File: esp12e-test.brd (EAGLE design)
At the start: 22.5 x 30.5 mm, 12 parts, among them IC1 ESP-12E/F, U8 NCP1117LPST50T3G

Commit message: Add button and STEMMA connectors to esp12e-test board
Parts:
- added JP1, JP2: (no value), microbuilder:1X04_1.0MM
- added U$1: AMAZON_BUTTON, 00jim:AMAZON_BUTTON
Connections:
- net GND: now also JP1.1, JP2.1, U$1.2, U$1.3
- net IO00: now also U$1.1, U$1.4
- net SCL: now also JP1.4, JP2.4
- net SDA: now also JP1.3, JP2.3
- net VCC: now also JP1.2, JP2.2
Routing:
- net IO00: track 29.0 -> 62.0 mm, vias 2 -> 1
- net VCC: track 54.7 -> 84.9 mm, vias 1 -> 4
- net GND: track 32.2 -> 58.0 mm, vias 2 -> 6
- net SCL: track 19.4 -> 39.5 mm, vias 0 -> 2
- net SDA: track 19.2 -> 33.0 mm, vias 0 -> 1
- net EN: track 26.6 -> 34.4 mm
- net RXI: track 26.0 -> 33.7 mm, vias 1 -> 0
- net TXO: track 28.3 -> 21.3 mm
- net IO15: track 23.4 -> 24.9 mm
- net RST: track 26.9 -> 26.2 mm
- net RAW: track 20.8 -> 20.2 mm, vias 1 -> 2
- net IO02: track 14.0 -> 14.2 mm, vias 2 -> 0
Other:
- board size 22.5 x 30.5 mm -> 27.6 x 30.5 mm

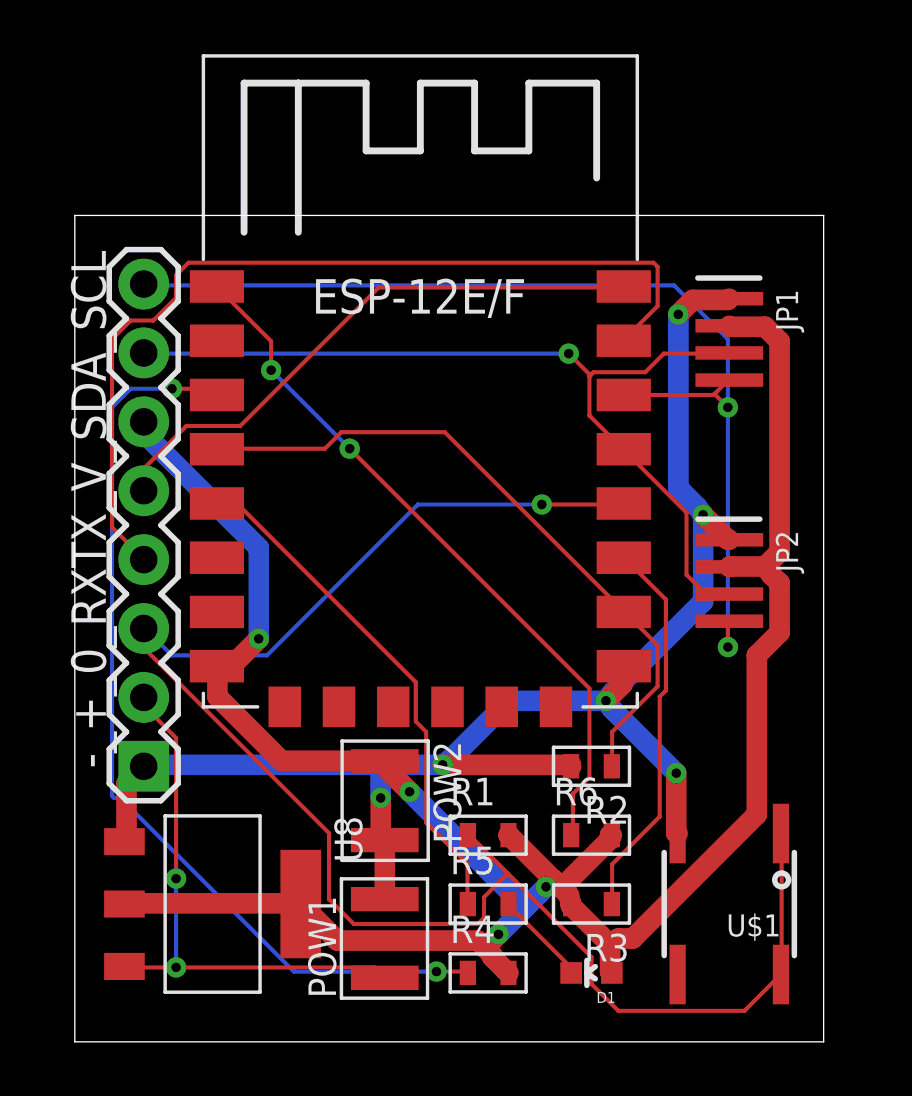
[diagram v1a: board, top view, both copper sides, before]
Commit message: Fix IO16 bug, change to better stemma-st connector
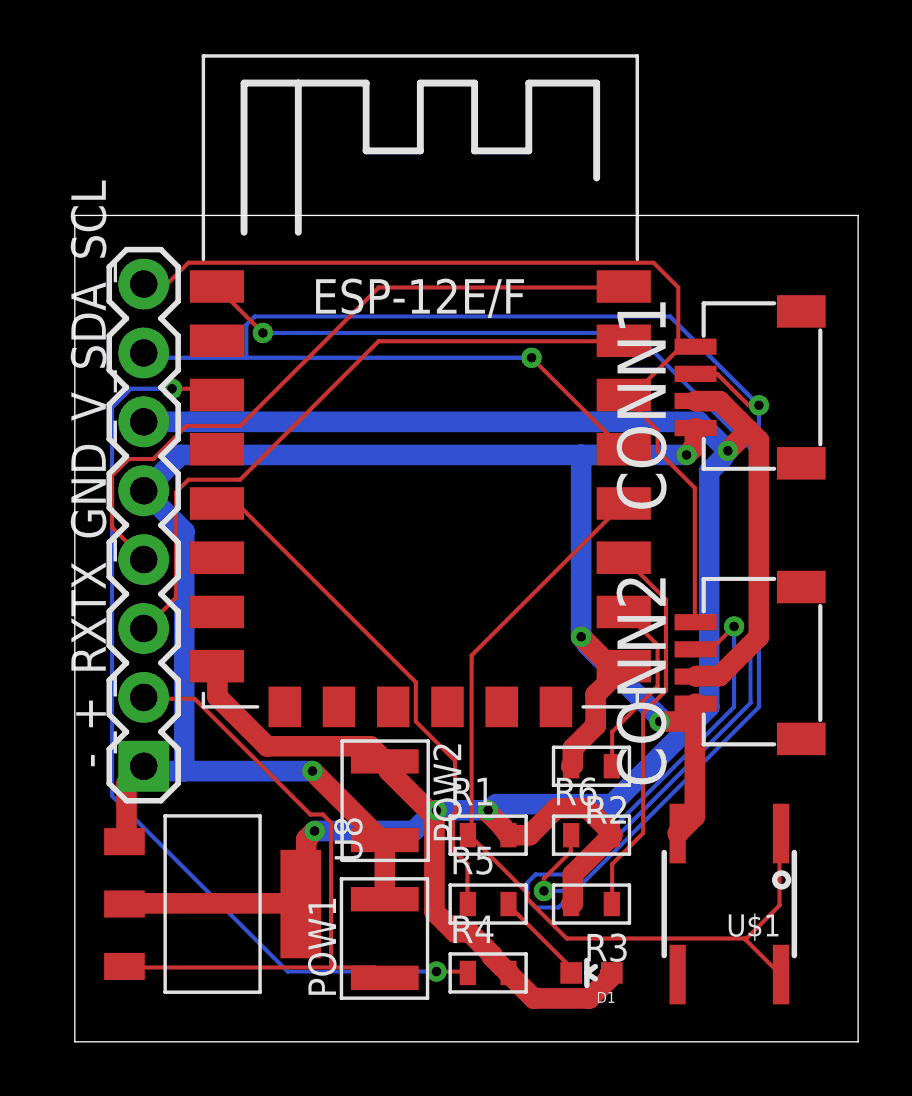
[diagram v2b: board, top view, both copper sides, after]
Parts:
- removed JP1, JP2: (no value), microbuilder:1X04_1.0MM
- added CONN1, CONN2: STEMMA_I2C_QT, 00jim:JST_SH4
- renumbered -_+_0_RXTX_V_SDA_SCL to -_+_RXTX_GND_V_SDA_SCL
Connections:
- net GND: now also -_+_RXTX_GND_V_SDA_SCL.5, CONN1.1, CONN2.1; no longer JP1.1, JP2.1
- net IO00: no longer -_+_RXTX_GND_V_SDA_SCL.3
- net IO15: no longer IC1.IO16
- net RXI: now also -_+_RXTX_GND_V_SDA_SCL.3; no longer -_+_RXTX_GND_V_SDA_SCL.4
- net SCL: now also CONN1.4, CONN2.4; no longer JP1.4, JP2.4
- net SDA: now also CONN1.3, CONN2.3; no longer JP1.3, JP2.3
- net TXO: now also -_+_RXTX_GND_V_SDA_SCL.4; no longer -_+_RXTX_GND_V_SDA_SCL.5
- net VCC: now also CONN1.2, CONN2.2; no longer JP1.2, JP2.2
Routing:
- net SDA: track 33.0 -> 82.1 mm, vias 1 -> 3
- net IO00: track 62.0 -> 32.9 mm, vias 1 -> 0
- net VCC: track 84.9 -> 103.9 mm
- net RST: track 26.2 -> 44.5 mm
- net IO15: track 24.9 -> 6.92 mm
- net GND: track 58.0 -> 71.8 mm, vias 6 -> 4
- net RXI: track 33.7 -> 24.4 mm
- net TXO: track 21.3 -> 25.3 mm
- net RAW: track 20.2 -> 23.9 mm, vias 2 -> 0
- net SCL: track 39.5 -> 36.2 mm, vias 2 -> 0
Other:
- board size 27.6 x 30.5 mm -> 28.9 x 30.5 mm
